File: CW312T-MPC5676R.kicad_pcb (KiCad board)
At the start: 2 copper layers, 58.7 x 53.7 mm, 83 parts, among them J1 DRB09P11G1R, J2 HDR_4_2.54, J3 2Pin_Header_2.54, J4 HDR_4_2.54, P1 PCIEx4 EDGE CONNECTOR, U1 SN65HVD232DR, U2 SN65HVD232DR, U3 SPC5676RDK3MVU1R, U4 LD1117STR

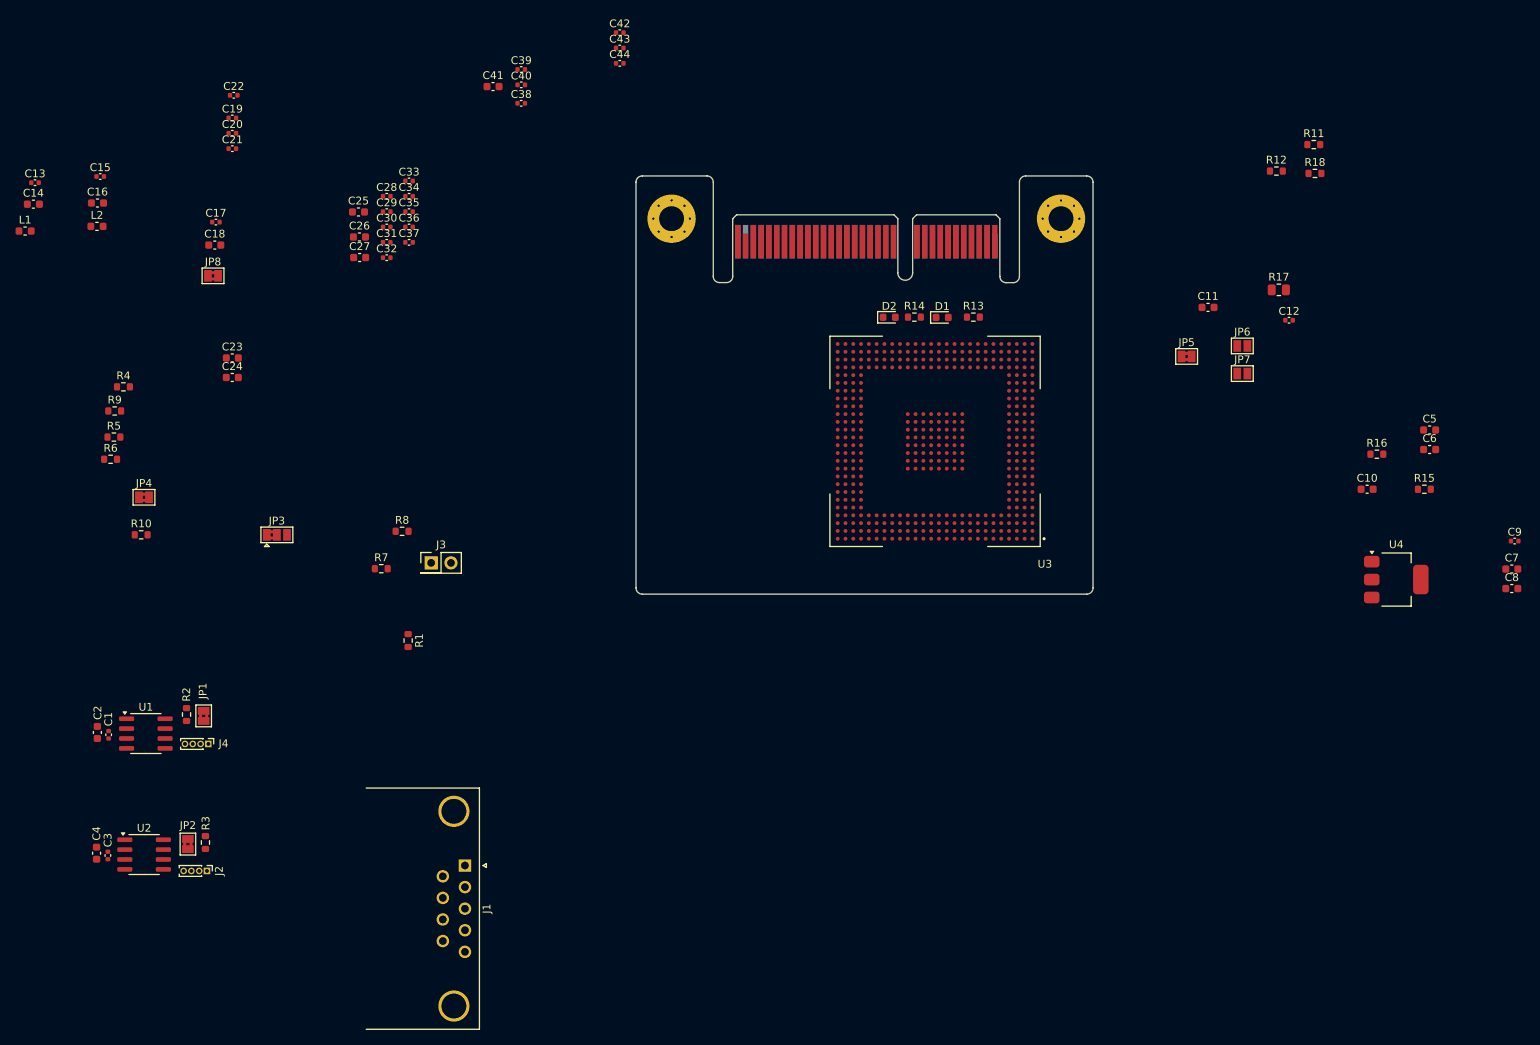
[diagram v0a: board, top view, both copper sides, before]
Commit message: updated schematic after library re-organization
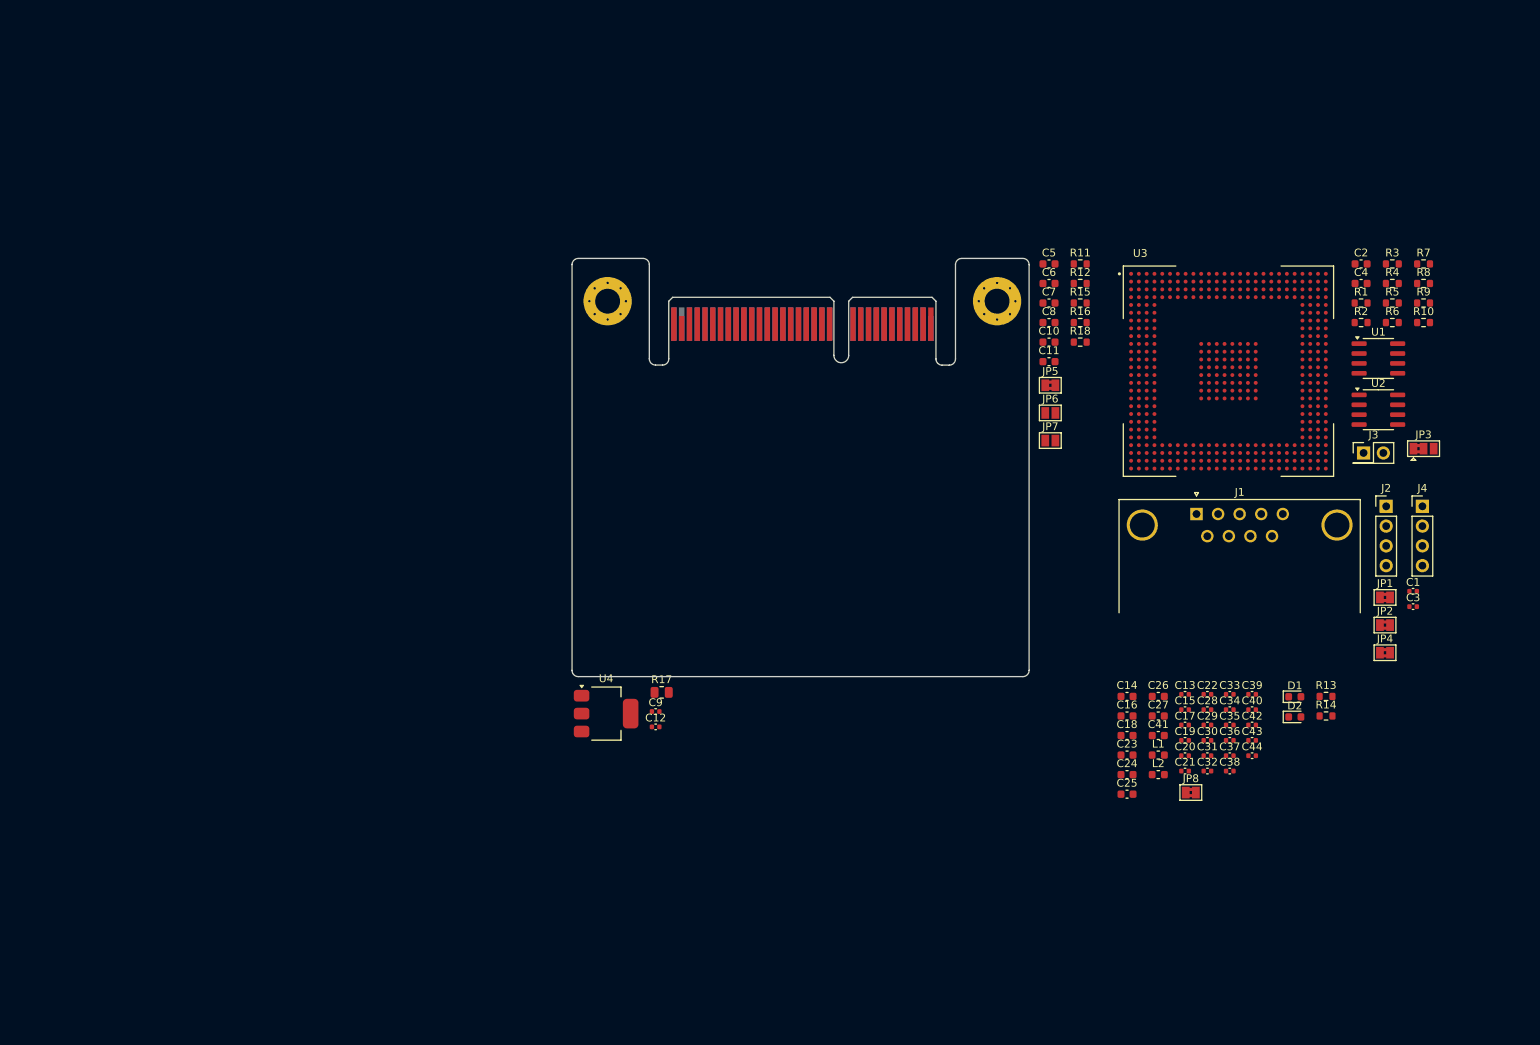
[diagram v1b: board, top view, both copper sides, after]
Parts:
- J2, J4: footprint Connector_PinHeader_1.00mm:PinHeader_1x04_P1.00mm_Vertical -> Connector_PinHeader_2.54mm:PinHeader_1x04_P2.54mm_Vertical
- moved C4 178.1 mm to (180.6, 60.2), turned to 0 degrees
- moved C2 173.0 mm to (180.6, 57.7), turned to 0 degrees
- moved C3 170.6 mm to (187.2, 101.7), turned to 0 degrees
- moved R3 169.5 mm to (184.6, 57.7), turned to 0 degrees
- moved R9 168.6 mm to (188.6, 62.7)
- moved C1 168.5 mm to (187.2, 99.8), turned to 0 degrees
- moved U2 168.4 mm to (182.8, 76.4)
- moved R10 166.9 mm to (188.6, 65.2)
- moved R6 165.5 mm to (184.6, 65.2)
- moved U1 165.4 mm to (182.8, 69.9)
- moved R5 165.0 mm to (184.6, 62.7)
- moved R4 163.4 mm to (184.6, 60.2)
- moved C13 161.6 mm to (157.9, 113.0)
- moved JP4 160.6 mm to (183.6, 107.6)
- moved L1 160.3 mm to (154.5, 120.8)
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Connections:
- JP1 pad 1: Net-(U1-CANH) -> Net-(JP1-Pad1)
- JP1 pad 2: Net-(JP1-Pad2) -> Net-(U1-CANH)
- JP2 pad 1: Net-(U2-CANH) -> Net-(JP2-Pad1)
- JP2 pad 2: Net-(JP2-Pad2) -> Net-(U2-CANH)
- R2 pad 1: Net-(JP1-Pad2) -> Net-(JP1-Pad1)
- R3 pad 1: Net-(JP2-Pad2) -> Net-(JP2-Pad1)
